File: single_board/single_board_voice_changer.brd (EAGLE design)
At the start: 58.1 x 48.2 mm, 26 parts, among them U1 ATMEGA328P_PDIP

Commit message: board with no ground plane, 0
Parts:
- moved JP1 80.2 mm to (57.1, 61.0), turned to 180 degrees
- moved INPUT1 50.9 mm to (3.81, 38.1), turned to 0 degrees
- moved INPUT2 47.0 mm to (3.81, 33.0), turned to 0 degrees
- moved INPUT3 43.6 mm to (3.81, 27.9), turned to 0 degrees
- moved JP2 43.4 mm to (17.8, 3.81), turned to 0 degrees
- moved INPUT4 41.0 mm to (3.81, 22.9), turned to 0 degrees
- moved IC1 39.9 mm to (54.6, 16.5), turned to 180 degrees
- moved LED 38.9 mm to (3.81, 5.08), turned to 180 degrees
- moved R3 38.1 mm to (10.2, 10.2)
- moved R6 37.7 mm to (25.4, 14.0), turned to 0 degrees
- moved ICSP 36.3 mm to (50.8, 35.6), turned to 0 degrees
- moved C6 32.1 mm to (15.2, 11.4), turned to 90 degrees
- moved EXT_LED 28.7 mm to (3.81, 17.8), turned to 270 degrees
- moved U$3 26.7 mm to (19.1, 36.8), turned to 0 degrees
- moved U$1 26.2 mm to (45.7, 53.3)
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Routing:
- net LED: track 107.8 -> 44.4 mm
- net GND: track 204.3 -> 241.2 mm
- net ADC_CH3: track 7.92 -> 36.2 mm
- net TX: track 42.2 -> 17.7 mm
- net MOSI: track 62.9 -> 38.4 mm, vias 1 -> 0
- net ADC_CH2: track 7.44 -> 29.4 mm
- net RX: track 38.0 -> 18.6 mm
- net ADC_CH1: track 6.99 -> 25.9 mm
- net N$1: track 20.4 -> 4.46 mm
- net ADC_CH0: track 7.58 -> 23.2 mm
- net VREF: track 73.6 -> 58.0 mm, vias 1 -> 0
- net N$2: track 22.8 -> 8.95 mm
- net MISO: track 39.0 -> 25.4 mm
- net N$4: track 15.3 -> 26.9 mm
- net LDAC: track 35.8 -> 45.5 mm
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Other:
- board size 58.1 x 48.2 mm -> 67 x 58.4 mm

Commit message: price down to 8.77
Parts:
- moved ICSP 35.6 mm to (15.2, 34.3)
- moved U$3 13.7 mm to (6.35, 41.9)
- moved JP1 6.35 mm to (50.8, 61.0)
- moved R6 5.08 mm to (20.3, 14.0)
- moved U$1 4.58 mm to (41.9, 50.8)
- moved C4 3.81 mm to (31.8, 8.89)
- moved C5 3.81 mm to (36.8, 8.89)
- moved XTAL 3.81 mm to (34.3, 14.0)
- moved C6 3.81 mm to (15.2, 7.62)
- moved INPUT2 2.84 mm to (2.54, 30.5)
- moved INPUT3 2.84 mm to (2.54, 25.4)
- moved EXT_LED 2.84 mm to (2.54, 15.2)
- moved JP2 2.84 mm to (15.2, 2.54)
- moved U$2 2.84 mm to (44.5, 39.4)
- moved IC1 2.84 mm to (52.1, 15.2)
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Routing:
- net RESET: track 71.7 -> 28.5 mm
- net GND: track 241.2 -> 225.3 mm
- net MISO: track 25.4 -> 39.3 mm
- net LDAC: track 45.5 -> 33.1 mm
- net MOSI: track 38.4 -> 42.5 mm
- net DTR: track 8.76 -> 5.13 mm
- net SCK: track 54.1 -> 50.8 mm
- net SS_ADC: track 15.0 -> 12.0 mm
- net N$4: track 26.9 -> 29.8 mm
- net ADC_CH2: track 29.4 -> 32.0 mm
- net VREF: track 58.0 -> 60.6 mm
- net ADC_CH1: track 25.9 -> 28.4 mm
- net ADC_CH0: track 23.2 -> 25.7 mm
- net ADC_CH3: track 36.2 -> 37.8 mm
- net RX: track 18.6 -> 19.9 mm
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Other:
- board size 67 x 58.4 mm -> 58.1 x 58.4 mm

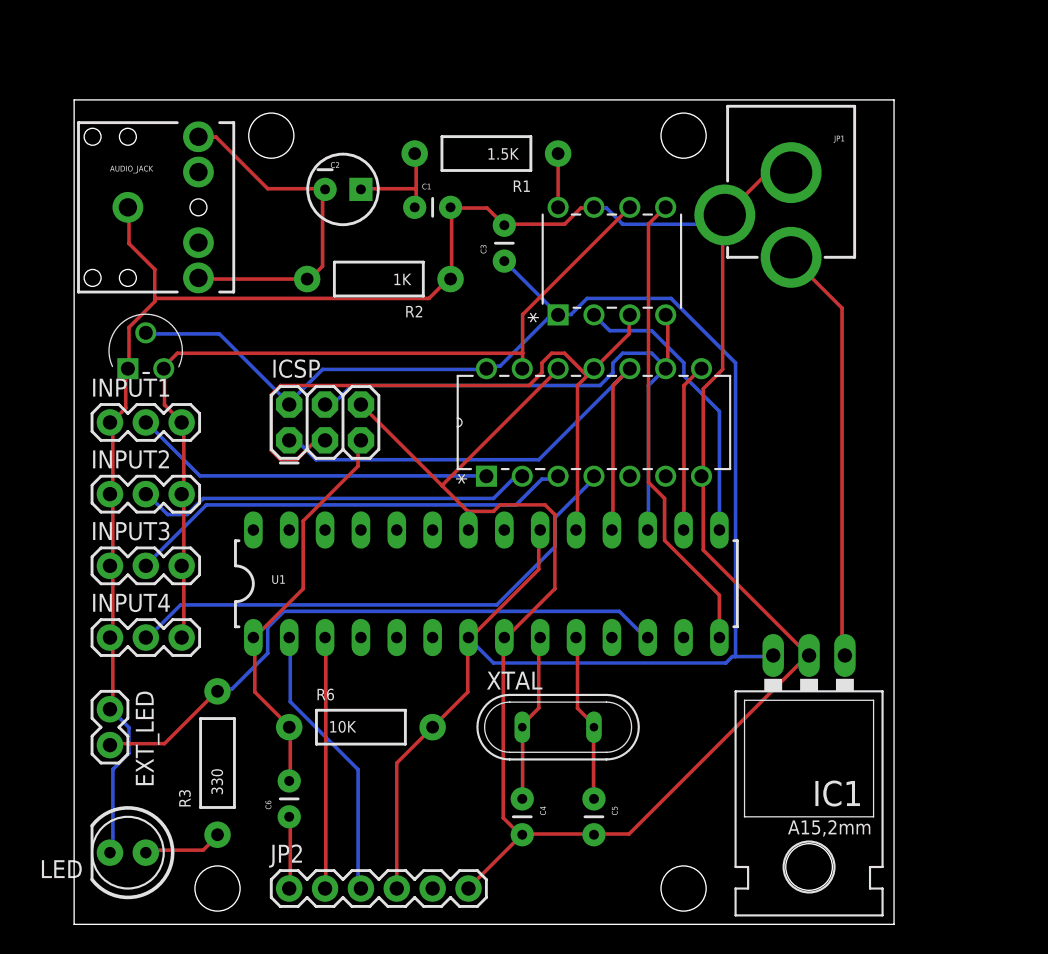
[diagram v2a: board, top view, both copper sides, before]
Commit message: change ADC to MCP3202
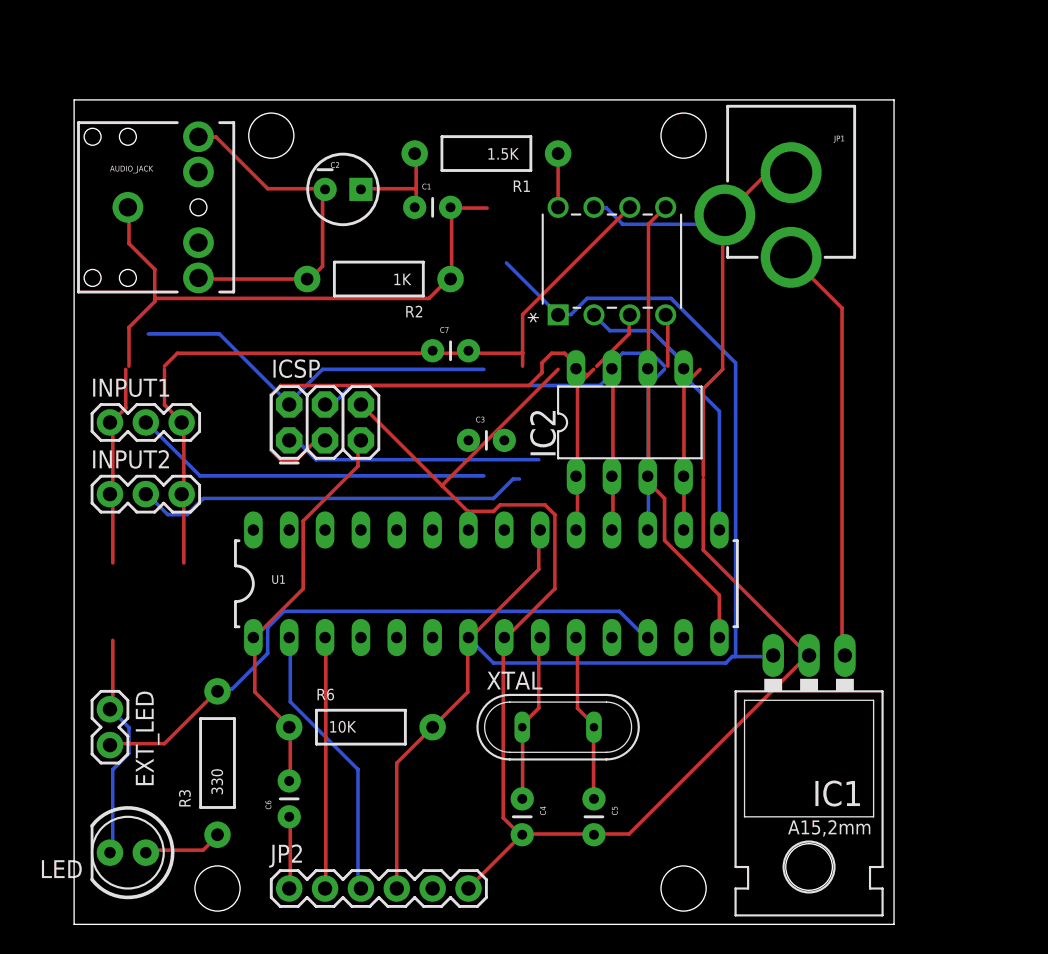
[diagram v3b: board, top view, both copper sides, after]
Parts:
- removed INPUT3, INPUT4: (no value), SparkFun-Connectors:1X03
- removed U$2: MCP3204-CI/P, Microchip_By_element14_Batch_1:DIP254P762X432-14
- removed U$3: MCP1702-3302E/TO, Microchip_By_element14_Batch_1:TO127P254X533-3
- added C7: 0.1uF, SparkFun-Passives:CAP-PTH-SMALL
- added IC2: MCP3202P, microchip:DIL8
- C3: device SparkFun-Capacitors:CAP-PTH-SMALL -> SparkFun-Passives:CAP-PTH-SMALL
- moved C3 13.0 mm to (27.9, 34.3), turned to 0 degrees
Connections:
- removed net ADC_CH2: INPUT3.2, U$2.3
- removed net ADC_CH3: INPUT4.2, U$2.4
- net ADC_CH0: now also IC2.2; no longer U$2.1
- net ADC_CH1: now also IC2.3; no longer U$2.2
- net GND: now also C7.2, IC2.4; no longer INPUT3.1, INPUT4.1, U$2.12, U$2.7, U$3.1
- net MISO: now also IC2.6; no longer U$2.10
- net MOSI: now also IC2.5; no longer U$2.9
- net SCK: now also IC2.7; no longer U$2.11
- net SS_ADC: now also IC2.1; no longer U$2.8
- net VCC: now also C7.1, IC2.8; no longer U$2.14, U$3.2
- net VREF: no longer INPUT3.3, INPUT4.3, U$2.13, U$3.3
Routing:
- net ADC_CH3: track 37.8 -> 0.00 mm
- net ADC_CH2: track 32.0 -> 0.00 mm
- net GND: track 225.3 -> 209.7 mm
- net MISO: track 39.3 -> 28.5 mm
- net VCC: track 127.6 -> 119.9 mm
- net VREF: track 60.6 -> 54.6 mm
- net SCK: track 50.8 -> 49.7 mm
- net MOSI: track 42.5 -> 42.0 mm

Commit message: redo board
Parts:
- moved JP1 75.5 mm to (-3.81, 8.89), turned to 270 degrees
- moved JP2 46.7 mm to (49.5, 34.3), turned to 270 degrees
- moved ICSP 42.7 mm to (49.5, 8.89), turned to 90 degrees
- moved IC1 32.7 mm to (20.3, 7.62), turned to 270 degrees
- moved C6 31.9 mm to (44.5, 20.3)
- moved R6 20.1 mm to (39.4, 7.62), turned to 270 degrees
- moved LED 17.6 mm to (12.7, 20.3), turned to 270 degrees
- moved IC2 15.9 mm to (25.4, 43.2)
- moved C4 14.8 mm to (24.1, 21.6)
- moved C1 14.0 mm to (38.1, 49.5)
- moved C3 13.7 mm to (39.4, 41.9), turned to 90 degrees
- moved R1 11.5 mm to (40.6, 53.3)
- moved C5 10.5 mm to (39.4, 19.1), turned to 90 degrees
- moved INPUT1 10.2 mm to (3.81, 25.4), turned to 90 degrees
- moved R2 9.16 mm to (26.7, 53.3)
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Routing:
- net SCK: track 49.7 -> 83.8 mm
- net RESET: track 28.5 -> 57.6 mm
- net N$4: track 29.8 -> 7.16 mm
- net MISO: track 28.5 -> 49.7 mm, vias 0 -> 1
- net RX: track 19.9 -> 40.4 mm
- net MOSI: track 42.0 -> 62.5 mm
- net N$2: track 7.80 -> 28.1 mm
- net TX: track 17.8 -> 36.4 mm
- net SS_DAC: track 20.7 -> 5.64 mm
- net GND: track 209.7 -> 195.8 mm
- net VCC: track 119.9 -> 131.6 mm
- net LED: track 43.8 -> 55.4 mm
- net DTR: track 5.13 -> 16.2 mm
- net LDAC: track 33.1 -> 23.0 mm
- net SS_ADC: track 11.9 -> 21.1 mm
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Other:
- board size 58.1 x 58.4 mm -> 53 x 55.9 mm

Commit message: another rev of the board design
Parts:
- moved INPUT2 54.3 mm to (49.5, 5.08), turned to 0 degrees
- moved ICSP 53.2 mm to (5.08, 38.1)
- moved JP2 49.0 mm to (2.54, 20.3), turned to 90 degrees
- moved INPUT1 48.2 mm to (49.5, 10.2), turned to 0 degrees
- moved EXT_LED 41.4 mm to (43.2, 5.08), turned to 180 degrees
- moved C6 38.1 mm to (6.35, 20.3), turned to 0 degrees
- moved R6 32.1 mm to (12.7, 25.4), turned to 90 degrees
- moved IC2 26.1 mm to (44.5, 25.4)
- moved C7 26.1 mm to (52.1, 26.7)
- moved R3 25.0 mm to (36.8, 21.6), turned to 90 degrees
- moved C1 19.2 mm to (19.1, 52.1)
- moved R1 14.5 mm to (26.7, 57.1)
- moved C3 12.0 mm to (29.2, 48.3)
- moved U$1 10.2 mm to (44.5, 55.9)
- moved C2 10.2 mm to (16.5, 57.1), turned to 0 degrees
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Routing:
- net GND: track 195.8 -> 0.00 mm
- net VCC: track 131.6 -> 0.00 mm
- net SCK: track 83.8 -> 0.00 mm
- net MOSI: track 62.5 -> 0.00 mm
- net VREF: track 59.5 -> 0.00 mm
- net RESET: track 57.6 -> 0.00 mm
- net LED: track 55.4 -> 0.00 mm
- net MISO: track 49.7 -> 0.00 mm, vias 1 -> 0
- net RX: track 40.4 -> 0.00 mm
- net TX: track 36.4 -> 0.00 mm
- net N$2: track 28.1 -> 0.00 mm
- net ADC_CH0: track 27.8 -> 0.00 mm
- net N$10: track 26.0 -> 0.00 mm
- net ADC_CH1: track 24.0 -> 0.00 mm
- net LDAC: track 23.0 -> 0.00 mm
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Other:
- board size 53 x 55.9 mm -> 60.6 x 63.5 mm

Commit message: another rev of the board design
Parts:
- moved EXT_LED 37.1 mm to (14.0, 27.9), turned to 270 degrees
- moved R3 16.5 mm to (20.3, 21.6)
- moved C7 14.4 mm to (41.9, 16.5), turned to 0 degrees
- moved INPUT2 10.2 mm to (39.4, 3.81)
- moved INPUT1 10.2 mm to (39.4, 10.2)
- moved LED 6.48 mm to (14.0, 19.1), turned to 0 degrees
- moved R6 5.08 mm to (7.62, 25.4)
- moved IC2 4.02 mm to (40.6, 24.1)
- moved XTAL 4.02 mm to (27.9, 24.1)
- moved C4 4.02 mm to (25.4, 19.1)
- moved C5 4.02 mm to (30.5, 19.1)
- moved AUDIO_JACK 3.81 mm to (3.81, 49.5)
- moved C3 3.81 mm to (33.0, 48.3)
- moved C2 3.81 mm to (16.5, 53.3)
- moved R1 3.81 mm to (26.7, 53.3)
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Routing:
- net GND: track 0.00 -> 179.8 mm
- net VCC: track 0.00 -> 115.1 mm
- net MOSI: track 0.00 -> 72.0 mm
- net SCK: track 0.00 -> 55.8 mm
- net VREF: track 0.00 -> 51.8 mm
- net MISO: track 0.00 -> 48.7 mm
- net LED: track 0.00 -> 28.6 mm
- net RESET: track 0.00 -> 27.7 mm
- net SS_ADC: track 0.00 -> 22.5 mm
- net LDAC: track 0.00 -> 21.4 mm
- net ADC_CH1: track 0.00 -> 20.9 mm
- net N$10: track 0.00 -> 20.5 mm
- net TX: track 0.00 -> 19.2 mm
- net N$5: track 0.00 -> 16.7 mm
- net RX: track 0.00 -> 15.7 mm
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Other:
- board size 60.6 x 63.5 mm -> 50.5 x 61 mm
- board text added: "Ultimate Voice Changer 2.0.0"
- board text added: "http://theotherandygrove.com"

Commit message: consistent fonts
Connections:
- net VCC: now also U$1.6
- net VREF: no longer U$1.6
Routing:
- net VREF: track 51.8 -> 6.48 mm
- net VCC: track 115.1 -> 124.9 mm
- net ADC_CH1: track 20.9 -> 20.0 mm
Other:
- board text added: "CH0"
- board text added: "CH1"
- board text added: "GND"
- board text added: "LED"
- board text added: "MCP3202"
- board text added: "MCP4921"
- board text added: "VCC"

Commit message: fix error with schematic
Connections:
- removed net VREF: INPUT1.3, INPUT2.3
- net VCC: now also INPUT1.3, INPUT2.3
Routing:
- net VREF: track 6.48 -> 0.00 mm
- net VCC: track 124.9 -> 131.2 mm
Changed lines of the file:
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@@
 <wire x1="7.0866" y1="31.0896" x2="7.62" y2="30.48" width="0.254" layer="1"/>
 <wire x1="26.5176" y1="33.147" x2="26.67" y2="33.02" width="0.254" layer="1"/>
+<contactref element="INPUT1" pad="3"/>
+<contactref element="INPUT2" pad="3"/>
+<wire x1="44.577" y1="10.0584" x2="44.577" y2="3.8862" width="0.254" layer="1"/>
+<wire x1="44.577" y1="3.8862" x2="44.45" y2="3.81" width="0.254" layer="1"/>
+<wire x1="44.577" y1="10.0584" x2="44.45" y2="10.16" width="0" layer="19" extent="1-1"/>
+<wire x1="41.91" y1="16.51" x2="44.45" y2="10.16" width="0" layer="19" extent="1-1"/>
 </signal>
 <signal name="SCK">
@@
 <wire x1="31.7754" y1="53.2638" x2="31.75" y2="53.34" width="0.254" layer="1"/>
 </signal>
-<signal name="VREF">
-<contactref element="INPUT1" pad="3"/>
-<contactref element="INPUT2" pad="3"/>
-<wire x1="44.577" y1="10.0584" x2="44.577" y2="3.8862" width="0.254" layer="1"/>
-<wire x1="44.577" y1="3.8862" x2="44.45" y2="3.81" width="0.254" layer="1"/>
-<wire x1="44.577" y1="10.0584" x2="44.45" y2="10.16" width="0.254" layer="1"/>
-</signal>
 <signal name="LDAC">
